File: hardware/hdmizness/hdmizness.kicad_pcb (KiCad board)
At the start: 2 copper layers, 85.6 x 54 mm, 66 parts, among them J1 HDMI_A_PCB, J2 USB_A_PCB, SW1 SW_Push, U1 F1C100s, U2 TDA19988, U3 W25Q128JVPIQ, U4 EA3058, Y1 24M

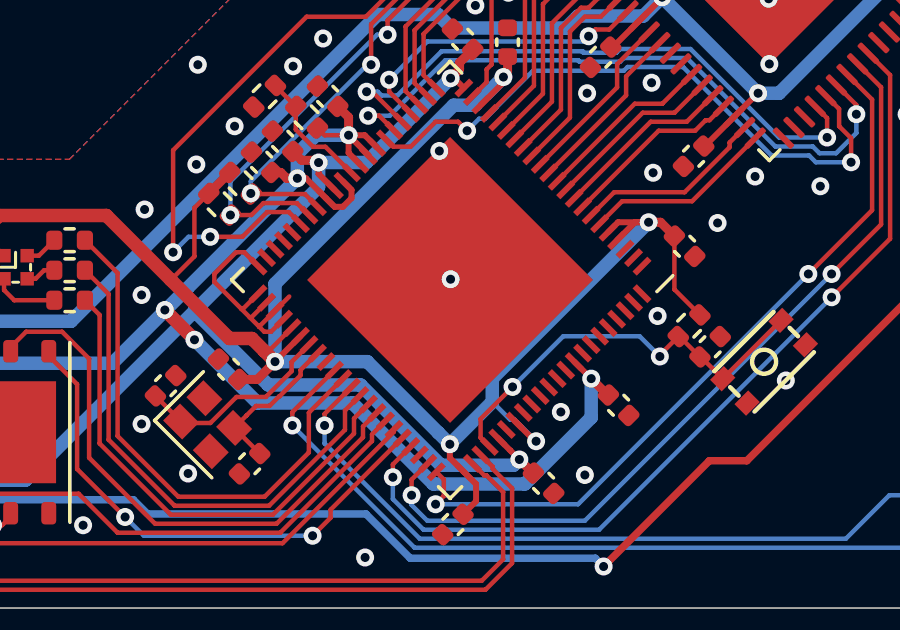
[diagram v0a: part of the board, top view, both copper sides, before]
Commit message: hdmizness: pcb: Add JLCPCB-specific string to set order number posision
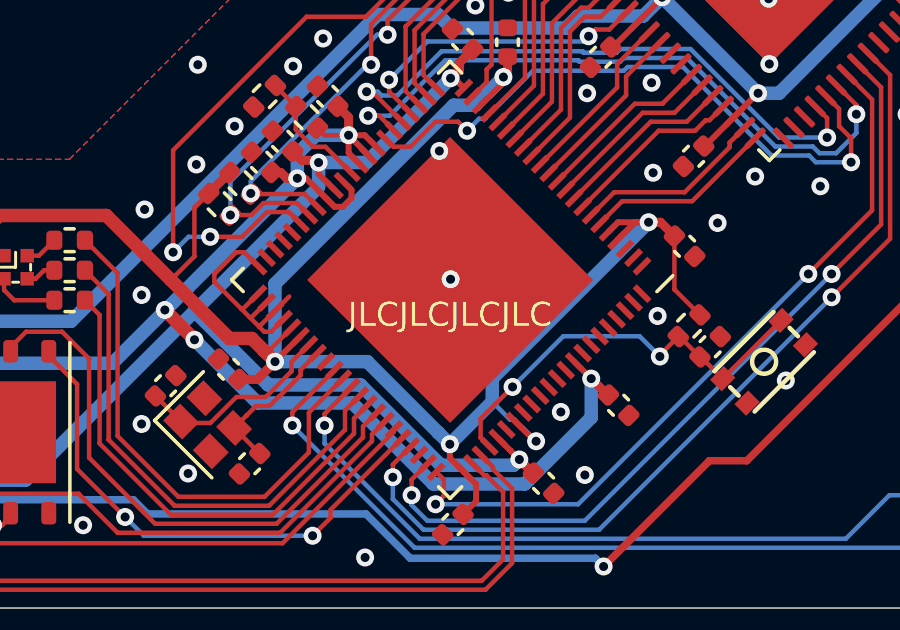
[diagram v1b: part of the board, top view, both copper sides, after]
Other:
- board text added: "JLCJLCJLCJLC"
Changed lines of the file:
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@@
   (general
     (thickness 0.8)
-    (drawings 19)
+    (drawings 20)
     (tracks 991)
     (zones 0)
@@
     )
   )
+  (gr_text JLCJLCJLCJLC (at 152.68 98.18) (layer F.SilkS)
+    (effects (font (size 0.8 0.8) (thickness 0.15)))
+  )
   (gr_text "Board version hard straps\nare not all directly connected to\nthe GND underneath the CPU\nfor easier bodging, if the need arises." (at 147.35 96.6) (layer Cmts.User)

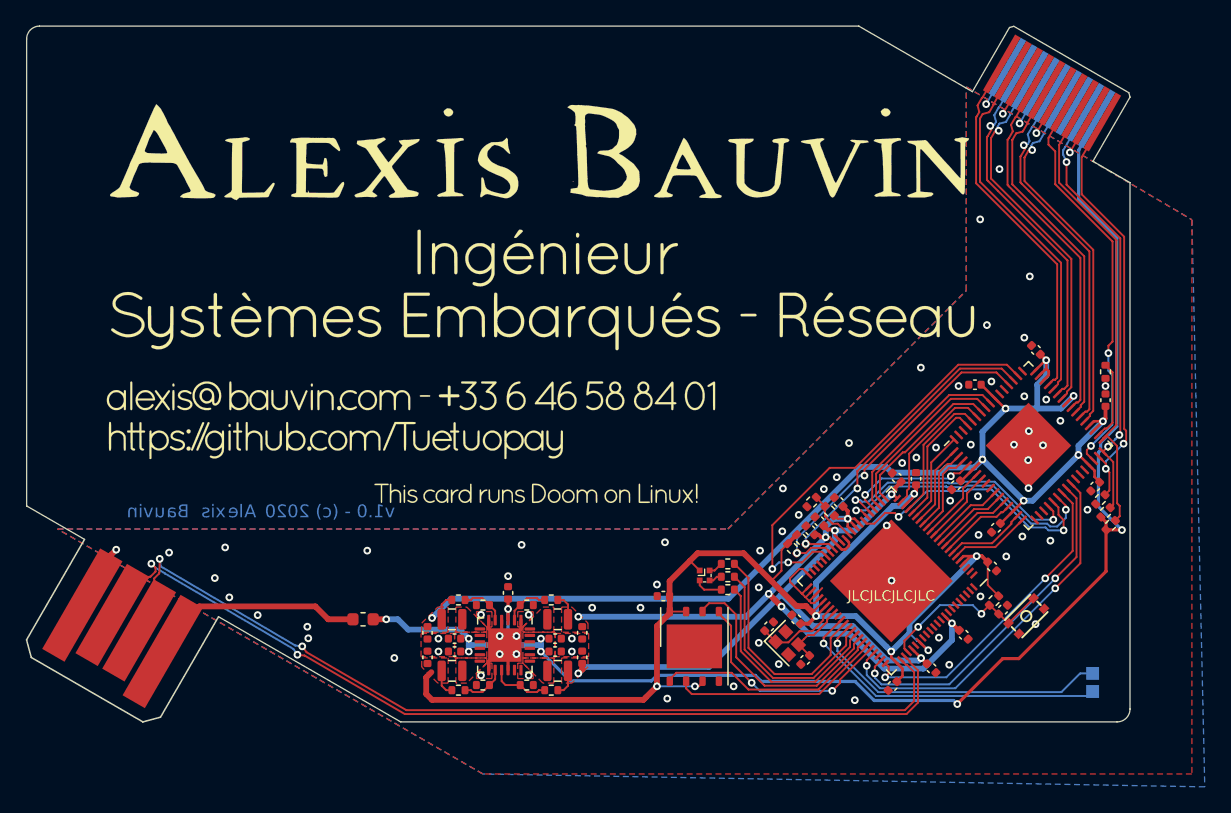
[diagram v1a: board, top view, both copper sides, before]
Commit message: hdmizness: Redo HDMI part with SiI9022A
Since I have a stock of 25 of both ICs...
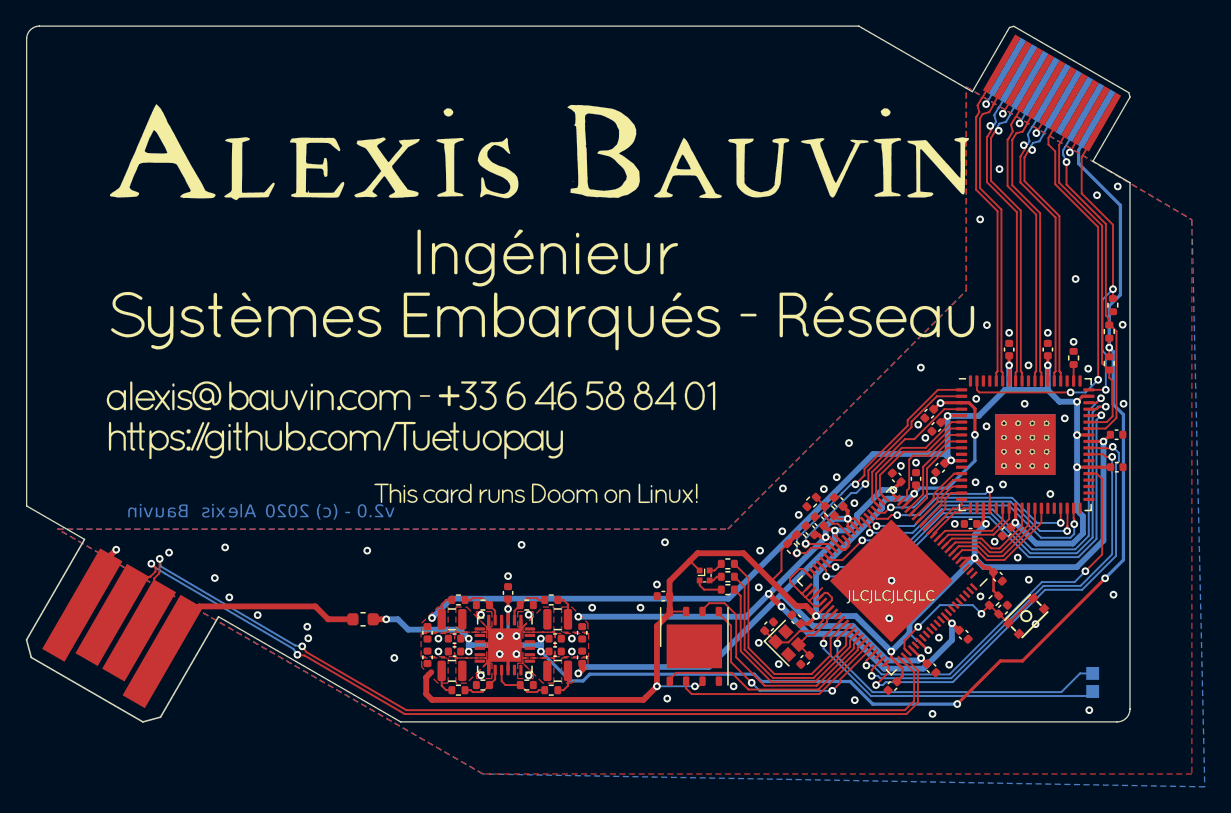
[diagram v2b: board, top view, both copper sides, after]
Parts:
- added C1: 100n, Capacitor_SMD:C_0402_1005Metric, F.Cu at (155.6, 84.0)
- added C31: 100n, Capacitor_SMD:C_0402_1005Metric, F.Cu at (158.8, 92.6)
- added C32: 100n, Capacitor_SMD:C_0402_1005Metric, F.Cu at (170.2, 85.7)
- R11: value 10k -> 4k3
- R15: value 200k -> 100k
- U2: value TDA19988 -> SiI9022A; footprint Package_DFN_QFN:QFN-64-1EP_9x9mm_P0.5mm_EP4.7x4.7mm -> hdmizness:QFN-72-1EP_10x10mm_P0.5mm_EP4.7x4.7mm_ThermalVias
- moved R10 15.1 mm to (169.9, 75.6), turned to 90 degrees
- moved R6 14.0 mm to (169.6, 77.7), turned to 270 degrees
- moved R7 12.6 mm to (169.6, 80.2), turned to 90 degrees
- moved C6 8.44 mm to (161.8, 79.1)
- moved C2 4.44 mm to (156.2, 85.1), turned to 45 degrees
- moved R11 2.70 mm to (166.8, 79.7), turned to 90 degrees
- moved C5 2.25 mm to (170.2, 88.2), turned to 180 degrees
- moved C3 1.82 mm to (156.5, 88.2)
- moved C7 0.93 mm to (164.8, 79.1), turned to 270 degrees
- moved C16 0.92 mm to (160.9, 96.7)
- moved C4 0.88 mm to (161.6, 93.2)
- moved U2 0.26 mm to (163.1, 86.5), turned to 0 degrees
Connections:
- C15 pad 1: +1V2 -> +1V1
- C17 pad 1: +1V2 -> +1V1
- C19 pad 1: +1V2 -> +1V1
- C2 pad 2: +1V8 -> +1V2
- C24 pad 2: +1V8 -> +1V2
- C3 pad 2: +1V8 -> +1V2
- C30 pad 2: +1V2 -> +1V1
- C4 pad 2: +1V8 -> +1V2
- C5 pad 2: +1V8 -> +1V2
- C6 pad 2: +1V8 -> +1V2
- C7 pad 2: +1V8 -> +1V2
- L2 pad 2: +1V8 -> +1V2
- L4 pad 2: +1V2 -> +1V1
- R15 pad 2: +1V8 -> +1V2
- R21 pad 2: +1V2 -> +1V1
- U1 pad 22: +1V2 -> +1V1
- U1 pad 35: +1V2 -> +1V1
- U1 pad 40: Net-(U1-Pad40) -> /HDMI_~RST
- U1 pad 41: Net-(U1-Pad41) -> /HDMI_CDC
- U1 pad 48: GND -> +3V3
- U1 pad 49: +3V3 -> GND
- U1 pad 71: +1V2 -> +1V1
- U2 pad 1: /RGB_D14 -> /CPU_SCL
- U2 pad 10: /RGB_D7 -> /RGB_D18
- U2 pad 11: /RGB_D6 -> GND
- U2 pad 12: /RGB_D5 -> +1V2
- U2 pad 13: /RGB_D4 -> GND
- U2 pad 14: +1V8 -> /RGB_D15
- U2 pad 15: /RGB_D3 -> /RGB_D14
- U2 pad 16: /RGB_D2 -> /RGB_D13
- U2 pad 17: GND -> /RGB_D12
- U2 pad 18: GND -> /RGB_D11
- U2 pad 19: GND -> /RGB_D10
- U2 pad 2: /RGB_D13 -> /CPU_SDA
- U2 pad 20: /RGB_DE -> GND
- U2 pad 21: /RGB_VSYNC -> +3V3
- U2 pad 22: /RGB_HSYNC -> /RGB_CLK
- U2 pad 23: /I2S_BCLK -> GND
- U2 pad 24: /I2S_LRCK -> /RGB_D7
- U2 pad 25: /I2S_DO -> /RGB_D6
- U2 pad 26: Net-(U2-Pad26) -> +1V2
- U2 pad 27: Net-(U2-Pad27) -> /RGB_D5
- U2 pad 28: Net-(U2-Pad28) -> /RGB_D4
- U2 pad 29: +1V8 -> /RGB_D3
- U2 pad 3: /RGB_D12 -> +3V3
- U2 pad 30: /HDMI_CEC -> /RGB_D2
- U2 pad 31: /HDMI_HPD -> GND
- U2 pad 32: /HDMI_SDA -> GND
- U2 pad 33: /HDMI_SCL -> /RGB_DE
- U2 pad 34: Net-(R11-Pad1) -> /RGB_HSYNC
- U2 pad 35: +1V8 -> /RGB_VSYNC
- U2 pad 36: +1V8 -> Net-(U2-Pad36)
- U2 pad 37: /HDMI_CK_N -> Net-(U2-Pad37)
- U2 pad 38: /HDMI_CK_P -> Net-(U2-Pad38)
- U2 pad 39: /HDMI_D0_N -> Net-(U2-Pad39)
- U2 pad 4: /RGB_CLK -> /RGB_D23
- U2 pad 40: /HDMI_D0_P -> Net-(U2-Pad40)
- U2 pad 41: +1V8 -> /I2S_DO
- U2 pad 42: /HDMI_D1_N -> +1V2
- U2 pad 43: /HDMI_D1_P -> GND
- U2 pad 44: /HDMI_D2_N -> /I2S_LRCK
- U2 pad 45: /HDMI_D2_P -> /I2S_BCLK
- U2 pad 46: +1V8 -> +3V3
- U2 pad 47: +1V8 -> +1V2
- U2 pad 48: +1V8 -> /HDMI_SDA
- U2 pad 49: GND -> /HDMI_SCL
- U2 pad 5: +1V8 -> +1V2
- U2 pad 50: /HDMI_INT -> /HDMI_CDC
- U2 pad 51: /CPU_SDA -> /HDMI_~RST
- U2 pad 52: /CPU_SCL -> /HDMI_INT
- U2 pad 53: GND -> +1V2
- U2 pad 54: GND -> /HDMI_HPD
- U2 pad 55: +1V8 -> GND
- U2 pad 56: /RGB_D23 -> Net-(R11-Pad1)
- U2 pad 57: /RGB_D22 -> GND
- U2 pad 58: /RGB_D21 -> /HDMI_CK_N
- U2 pad 59: /RGB_D20 -> /HDMI_CK_P
- U2 pad 6: /RGB_D11 -> /RGB_D22
- U2 pad 60: /RGB_D19 -> +1V2
- U2 pad 61: /RGB_D18 -> /HDMI_D0_N
- U2 pad 62: GND -> /HDMI_D0_P
- U2 pad 64: /RGB_D15 -> /HDMI_D1_N
- U2 pad 65: GND -> /HDMI_D1_P
- U2 pad 7: /RGB_D10 -> /RGB_D21
- U2 pad 8: GND -> /RGB_D20
- U2 pad 9: GND -> /RGB_D19
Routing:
- net +1V8: track 97.5 -> 0.00 mm, vias 8 -> 0
- net +1V1: track 0.00 -> 52.6 mm, vias 0 -> 4
- net +1V2: track 52.2 -> 96.7 mm, vias 4 -> 9
- net +3V3: track 104.6 -> 145.3 mm, vias 7 -> 11
- net /HDMI_~RST: track 0.00 -> 36.9 mm, vias 0 -> 2
- net /HDMI_CDC: track 0.00 -> 36.7 mm, vias 0 -> 2
- net /I2S_BCLK: track 24.8 -> 35.6 mm
- net /HDMI_HPD: track 32.9 -> 24.7 mm
- net /HDMI_SCL: track 35.9 -> 28.0 mm
- net /I2S_LRCK: track 27.2 -> 33.7 mm
- net /HDMI_SDA: track 33.9 -> 28.4 mm, vias 3 -> 1
- net /CPU_SDA: track 25.5 -> 20.2 mm
- net Net-(R11-Pad1): track 6.18 -> 1.28 mm
- net /HDMI_CK_N: track 28.7 -> 24.3 mm
- net /CPU_SCL: track 26.5 -> 22.2 mm
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- added copper zone on F.Cu, net +1V1
- removed copper zone on F.Cu, net +1V8
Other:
- board text added: "v2.0 - (c) 2020"
- board text removed: "v1.0 - (c) 2020"
